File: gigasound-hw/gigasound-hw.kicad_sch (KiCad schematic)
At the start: 75 parts, among them J1 Conn_01x04_Socket, J2 Conn_01x05_Socket, J3 Conn_01x05_Socket, J4 USB_C_Receptacle_USB2.0_16P, J5 PIN_LED_OUT, SW1 PLAY, SW2 100nF, SW4 STOP, SW5 MODE, U1 STM32F401RETx, U5 AMS1117-3.3, Y1 8MHz

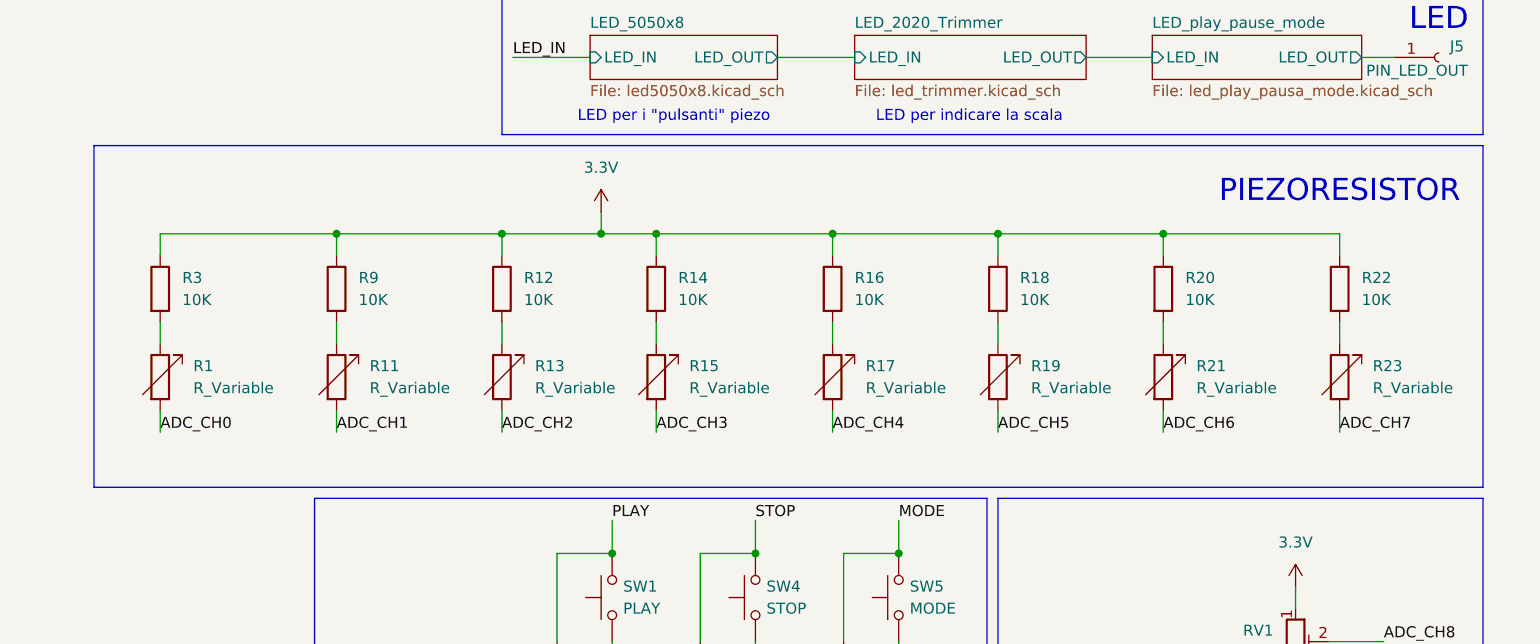
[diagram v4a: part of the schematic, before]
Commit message: fix GIGA error
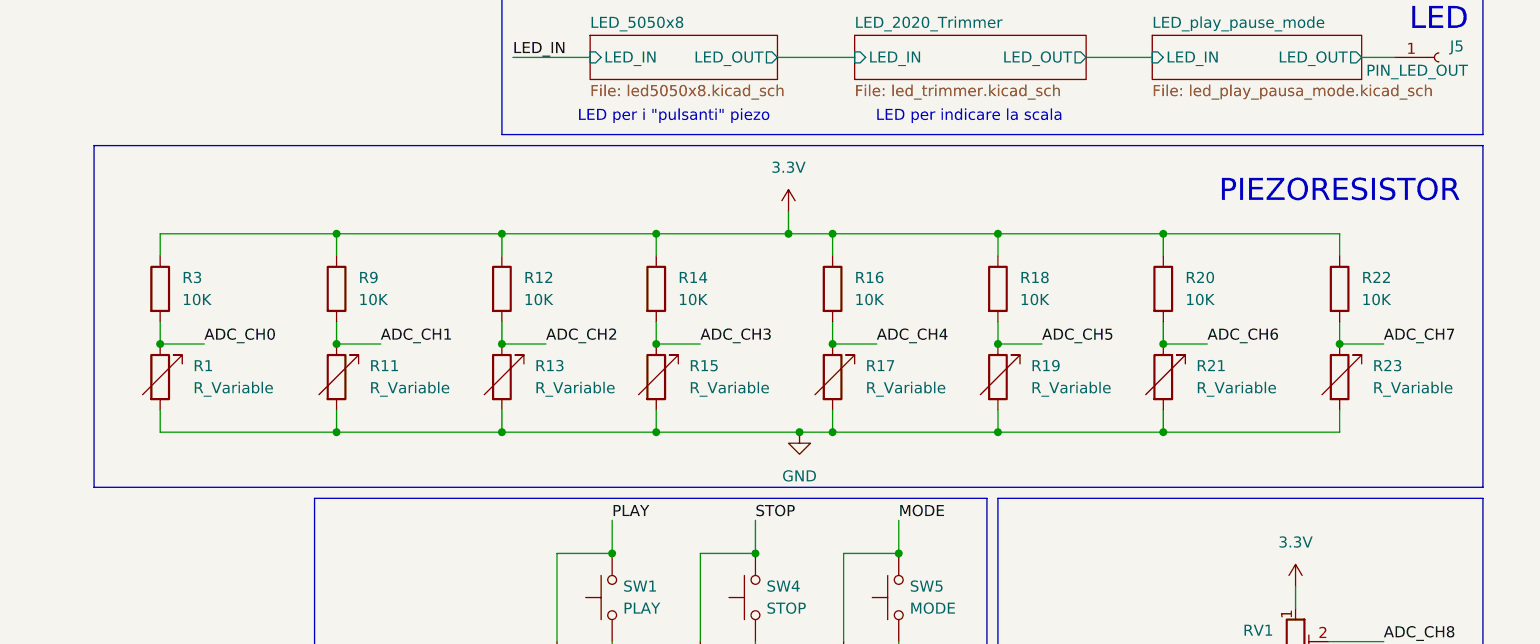
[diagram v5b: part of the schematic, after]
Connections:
- net ADC_CH0: now also R1.1, R3.2; no longer R1.2
- net ADC_CH1: now also R11.1, R9.2; no longer R11.2
- net ADC_CH2: now also R12.2, R13.1; no longer R13.2
- net ADC_CH3: now also R14.2, R15.1; no longer R15.2
- net ADC_CH4: now also R16.2, R17.1; no longer R17.2
- net ADC_CH5: now also R18.2, R19.1; no longer R19.2
- net ADC_CH6: now also R20.2, R21.1; no longer R21.2
- net ADC_CH7: now also R22.2, R23.1; no longer R23.2
- net GND: now also R1.2, R11.2, R13.2, R15.2, R17.2, R19.2, R21.2, R23.2
